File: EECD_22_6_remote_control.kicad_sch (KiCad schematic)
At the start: 29 parts, among them SW1 SW_SPDT, U1 NRF24L01_Breakout, U1 STM32L4P5RET6, U2(buck-boost) LTC3440EMS

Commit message: Apply custom drawing sheet and project settings
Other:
- company: (none) -> Authors: A. Kotkov, I. Kajdan
- title: (none) -> RC Helicopter Remote Control
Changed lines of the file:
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@@
 (kicad_sch (version 20211123) (generator eeschema)
   (paper "A4")
+  (title_block
+    (title "RC Helicopter Remote Control")
+    (date "2022-12-28")
+    (rev "${REVISION}")
+    (company "Authors: A. Kotkov, I. Kajdan")
+    (comment 1 "Reviewer: A. Bondyra")
+  )
   (junction (at 120.65 68.58) (diameter 0) (color 0 0 0 0)
   )

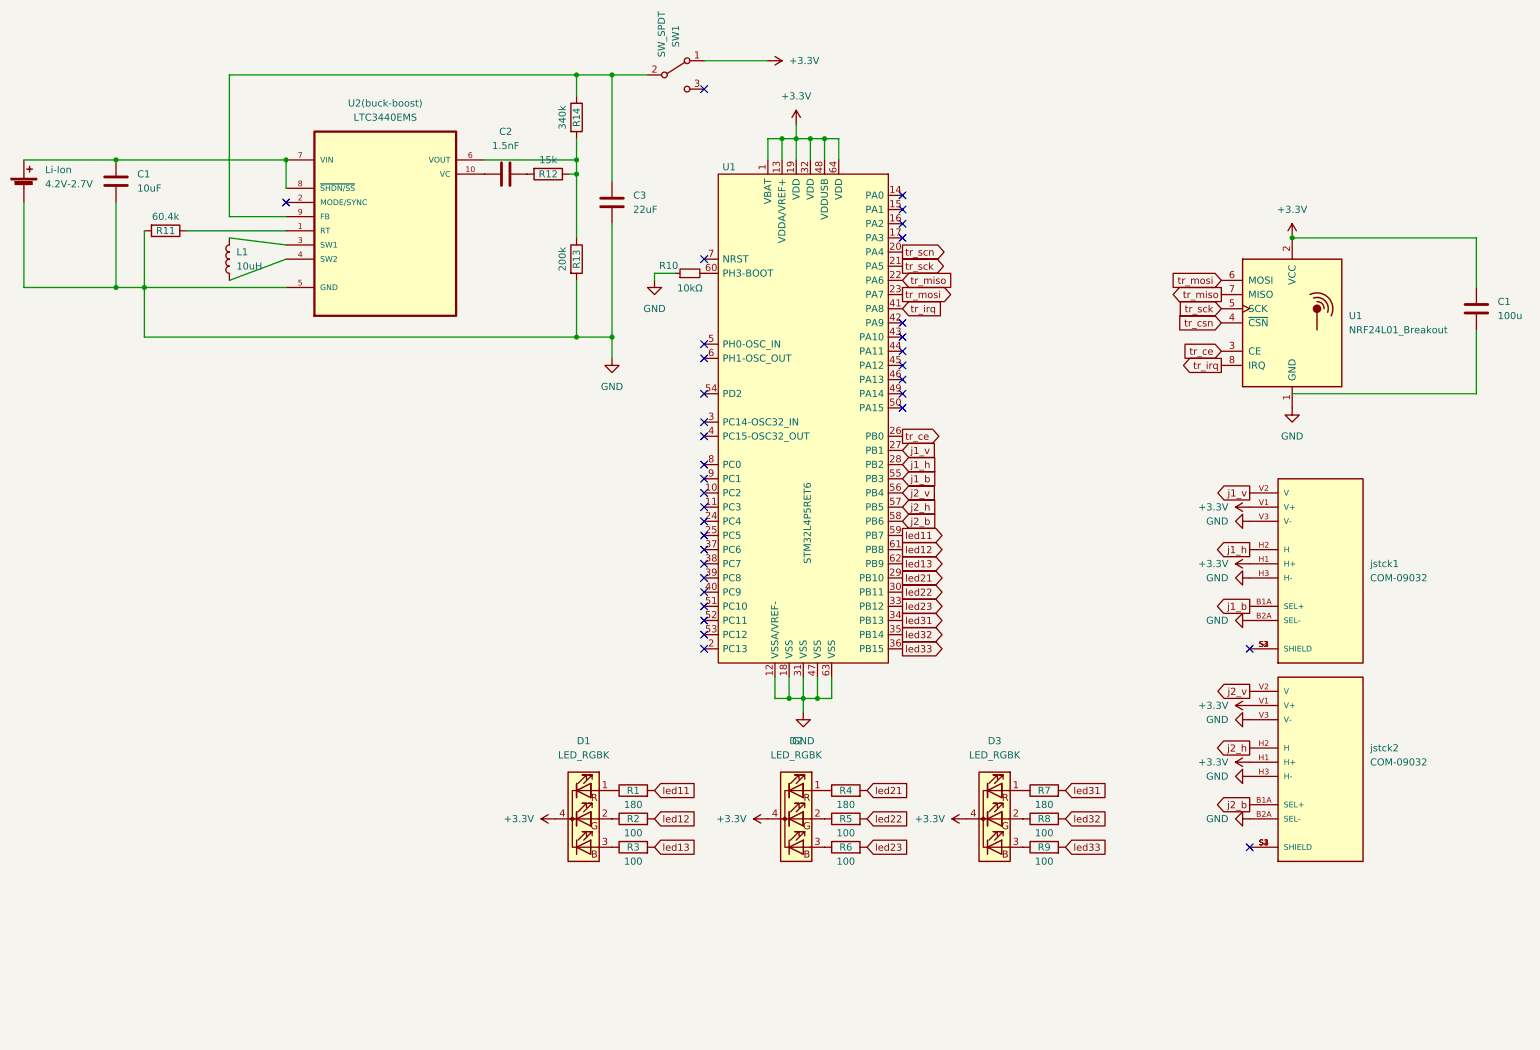
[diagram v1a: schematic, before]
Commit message: Schematic refactor
- Divide the schematic into hierarchical sheets
- Fix ERCs
- Remove unused footprints
- Add SWD connector
- Add bypass capacitors
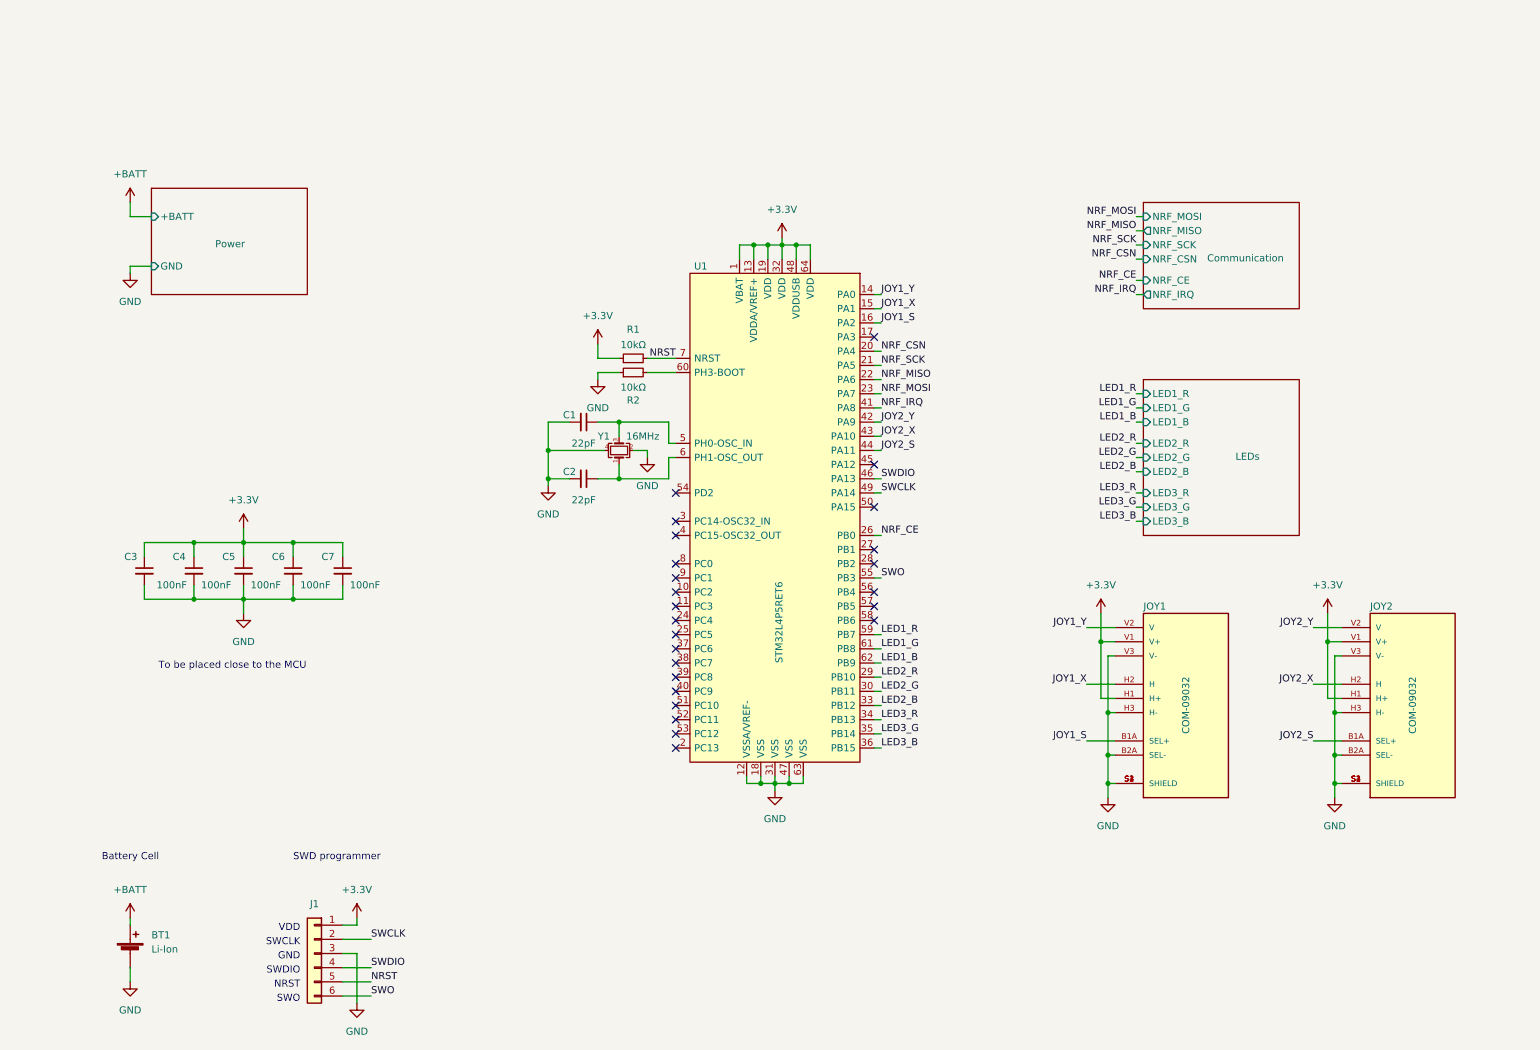
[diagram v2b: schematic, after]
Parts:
- removed C1: 100u, Capacitor_SMD:C_0201_0603Metric, symbol Device:C
- removed C1: 10uF, Capacitor_THT:CP_Axial_L10.0mm_D4.5mm_P15.00mm_Horizontal, symbol Device:C
- removed C2: 1.5nF, Capacitor_THT:CP_Axial_L10.0mm_D4.5mm_P15.00mm_Horizontal, symbol Device:C
- removed C3: 22uF, Capacitor_THT:CP_Axial_L10.0mm_D4.5mm_P15.00mm_Horizontal, symbol Device:C
- removed D1, D2, D3: LED_RGBK, LED_SMD:LED_Avago_PLCC4_3.2x2.8mm_CW, symbol Device:LED_RGBK
- removed L1: 10uH, Inductor_SMD:L_6.3x6.3_H3, symbol Device:L
- removed Li-Ion: 4.2V-2.7V, symbol Device:Battery_Cell
- removed R1, R4, R7: 180, Resistor_SMD:R_0201_0603Metric, symbol Device:R
- removed R10: 10kΩ, Resistor_SMD:R_0603_1608Metric, symbol Device:R_Small
- removed R11: 60.4k, Resistor_SMD:R_0201_0603Metric, symbol Device:R
- removed R12: 15k, Resistor_SMD:R_0201_0603Metric, symbol Device:R
- removed R13: 200k, Resistor_SMD:R_0201_0603Metric, symbol Device:R
- removed R14: 340k, Resistor_SMD:R_0201_0603Metric, symbol Device:R
- removed R2, R3, R5, R6, R8, R9: 100, Resistor_SMD:R_0201_0603Metric, symbol Device:R
- removed SW1: SW_SPDT, Button_Switch_THT:SW_CuK_JS202011CQN_DPDT_Straight, symbol Switch:SW_SPDT
- removed U1: NRF24L01_Breakout, RF_Module:nRF24L01_Breakout, symbol RF:NRF24L01_Breakout
- removed U1: STM32L4P5RET6, Package_QFP:LQFP-64_10x10mm_P0.5mm, symbol Local_Library:STM32L4P5RET6
- removed U2(buck-boost): LTC3440EMS, models:SON50P300X300X80-11N-D, symbol LTC3440EMS:LTC3440EMS
- removed jstck1, jstck2: COM-09032, models:XDCR_COM-09032, symbol COM-09032:COM-09032
- added BT1: Li-Ion, Local_Library:BAT_BCAAAW, symbol Device:Battery_Cell
- added C1, C2: 22pF, Capacitor_SMD:C_0603_1608Metric, symbol Device:C_Small
- added C3, C4, C5, C6, C7: 100nF, Capacitor_SMD:C_0603_1608Metric, symbol Device:C_Small
- added J1: SWD, Connector_PinHeader_2.54mm:PinHeader_2x03_P2.54mm_Vertical, symbol Connector_Generic:Conn_01x06
- added JOY1, JOY2: COM-09032, XDCR_COM-09032, symbol COM-09032:COM-09032
- added R1, R2: 10kΩ, Resistor_SMD:R_0603_1608Metric, symbol Device:R_Small
- added U1: STM32L4P5RET6, Package_QFP:LQFP-64_10x10mm_P0.5mm, symbol STM32L4P5RET6:STM32L4P5RET6
- added Y1: 16MHz, Crystal:Crystal_SMD_3225-4Pin_3.2x2.5mm, symbol Device:Crystal_GND24_Small
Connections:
- net +3.3V: now also C3.1, C4.1, C5.1, C6.1, C7.1, J1.1 (Pin_1), JOY1.H1 (H+), JOY1.V1 (V+), JOY2.H1 (H+), JOY2.V1 (V+), R1.1, U1.1 (VBAT), U1.13 (VDDA/VREF+), U1.19 (VDD), U1.32 (VDD), U1.48 (VDDUSB), U1.64 (VDD)
- net GND: now also BT1.2 (-), C1.2, C2.2, C3.2, C4.2, C5.2, C6.2, C7.2, J1.3 (Pin_3), JOY1.B2A (SEL-), JOY1.H3 (H-), JOY1.S1 (SHIELD), JOY1.S2 (SHIELD), JOY1.S3 (SHIELD), JOY1.S4 (SHIELD), JOY1.V3 (V-), JOY2.B2A (SEL-), JOY2.H3 (H-), JOY2.S1 (SHIELD), JOY2.S2 (SHIELD), JOY2.S3 (SHIELD), JOY2.S4 (SHIELD), JOY2.V3 (V-), R2.1, U1.12 (VSSA/VREF-), U1.18 (VSS), U1.31 (VSS), U1.47 (VSS), U1.63 (VSS), Y1.2, Y1.4
- new net: C2.1, U1.6 (PH1-OSC_OUT), Y1.1
- new net: C1.1, U1.5 (PH0-OSC_IN), Y1.3
- new net: R2.2, U1.60 (PH3-BOOT)
- new net +BATT: BT1.1 (+)
- new net JOY1_S: JOY1.B1A (SEL+), U1.16 (PA2)
- new net JOY1_X: JOY1.H2 (H), U1.15 (PA1)
- new net JOY1_Y: JOY1.V2 (V), U1.14 (PA0)
- new net JOY2_S: JOY2.B1A (SEL+), U1.44 (PA11)
- new net JOY2_X: JOY2.H2 (H), U1.43 (PA10)
- new net JOY2_Y: JOY2.V2 (V), U1.42 (PA9)
- new net LED1_B: U1.62 (PB9)
- new net LED1_G: U1.61 (PB8)
- new net LED1_R: U1.59 (PB7)
- new net LED2_B: U1.33 (PB12)
- new net LED2_G: U1.30 (PB11)
- new net LED2_R: U1.29 (PB10)
- new net LED3_B: U1.36 (PB15)
- new net LED3_G: U1.35 (PB14)
- new net LED3_R: U1.34 (PB13)
- new net NRF_CE: U1.26 (PB0)
- new net NRF_CSN: U1.20 (PA4)
- new net NRF_IRQ: U1.41 (PA8)
- new net NRF_MISO: U1.22 (PA6)
- new net NRF_MOSI: U1.23 (PA7)
- new net NRF_SCK: U1.21 (PA5)
- new net NRST: J1.5 (Pin_5), R1.2, U1.7 (NRST)
- new net SWCLK: J1.2 (Pin_2), U1.49 (PA14)
- new net SWDIO: J1.4 (Pin_4), U1.46 (PA13)
- new net SWO: J1.6 (Pin_6), U1.55 (PB3)
- no-connect marks 35 -> 25
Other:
- added sheet Communication (communication.kicad_sch)
- added sheet LEDs (leds.kicad_sch)
- added sheet Power (power.kicad_sch)
- note added: "Battery Cell"
- note added: "GND"
- note added: "NRST"
- note added: "SWCLK"
- note added: "SWD programmer"
- note added: "SWDIO"
- note added: "SWO"
- note added: "To be placed close to the MCU"
- note added: "VDD"
